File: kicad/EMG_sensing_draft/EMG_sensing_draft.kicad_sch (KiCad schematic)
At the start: 68 parts, among them J1 EMG_SIGNAL, J2 USB_A_0480370001, J3 DEBUG, U1 W25Q128JV, U2 RN4871-I/RM140, U3 RP2040, U4 MCP1702T-3302E_CB, U5 NCS4325DR2G, U6 MCP6021, U7 MCP6N11-002E/SN, Y1 12MHz

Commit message: restructured repo
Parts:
- removed C12: 0.1uF, symbol Device:C
- removed C13: 10uF, symbol Device:C
- removed C15: .33uF, symbol Device:C
- removed R21: 453, symbol Device:R
- removed R22: 200, symbol Device:R
- removed R23: 10k, symbol Device:R
- removed U5: NCS4325DR2G, SOIC14_4X8P75_ONS, symbol NCS4325DR2G:NCS4325DR2G
- added C17: 0.1uF, symbol Device:C
- added C21, C23: .33uF, symbol Device:C
- added C22: .033uF, symbol Device:C
- added R19: 9.09k, symbol Device:R
- added R25: 453, symbol Device:R
- added R26: 200, symbol Device:R
- added U7: MCP6024-I/P, PDIP14_300MC_MCH, symbol MCP6024:MCP6024-I/P
- C16: value .033uF -> 1uF
- C18: value .33uF -> 1uF
- C19: value 1uF -> .1uF
- C20: value .1uF -> 10uF
- R14: value 453 -> 10k
- R15: value 909 -> 453
- R16: value 8.1K -> 10k
- R17: value 9.09k -> 909
- R18: value 200 -> 8.1K
- R20: value 909 -> 200
- R24: value 10k -> 909
- renumbered C21 to C12, C22 to C13, C17 to C15, J2 to J1, J1 to J2, R25 to R10, R26 to R11, R19 to R12, R10 to R21, R11 to R22, R12 to R23, U2 to U1, U1 to U2, U7 to U4, U4 to U5
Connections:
- net +1.65V: now also R14.2, R15.1, R16.2, U7.12 (VIND+), U7.3 (VINA+); no longer R14.1, R24.2
- net +3.3V: now also C16.2, C18.1, C17.2, U7.4 (VDD); no longer C20.1
- net GND: now also R16.1, C17.1, C22.1, C23.2, U7.11 (VSS); no longer C20.2, R20.1
- net V_SIGNAL: now also C22.2, R19.2; no longer C16.2, R17.2
- net at R20.2: now also R26.1, U7.13 (VIND-); no longer C18.1
- net at R18.1: now also C20.2, U7.2 (VINA-); no longer R16.2
- net at R18.2: now also R20.1, U7.1 (VOUTA)
- net at R13.2: now also C20.1
- net at D7.2 (K): now also R26.2, U7.10 (VINC+)
- net at D7.1 (A): now also U7.14 (VOUTD)
- net at R15.2, R17.1: now also C21.1, U7.6 (VINB-)
- net at U6.1, U6.4: now also R14.1
- new net: C21.2, R17.2, R19.1, U7.7 (VOUTB)
- new net: C23.1, R24.2, R25.1, U7.5 (VINB+)
- new net: R25.2, U7.8 (VOUTC), U7.9 (VINC-)
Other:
- note added: "BANDPASS FILTER, RECTIFICATION, AND LEVEL SHIFTING"
- note added: "REFERENCE VOLTAGE"
- note removed: "BANDPASS FILTER AND RECTIFICATION"
- moved on the sheet: C12, C13, C14, C15, D1, D6, J1, J2, J3, R10, R11, R12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

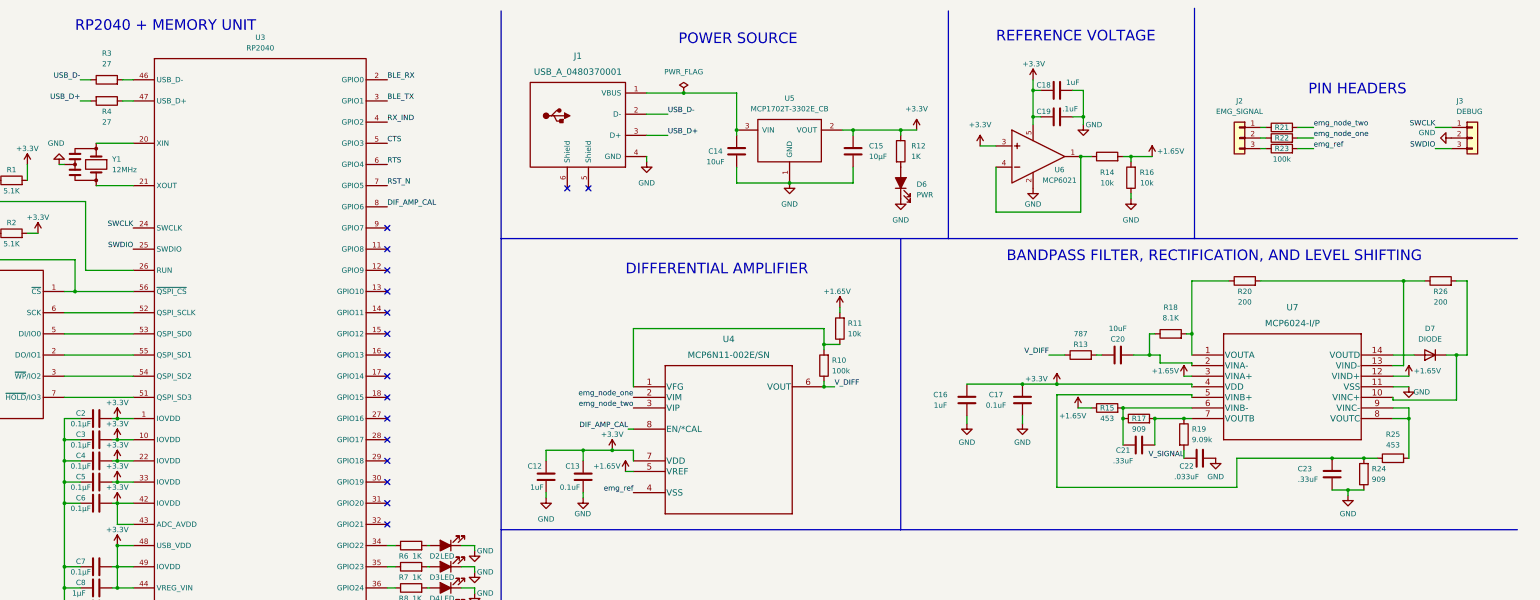
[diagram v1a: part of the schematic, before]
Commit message: fixed mcp6024 schematic symbol
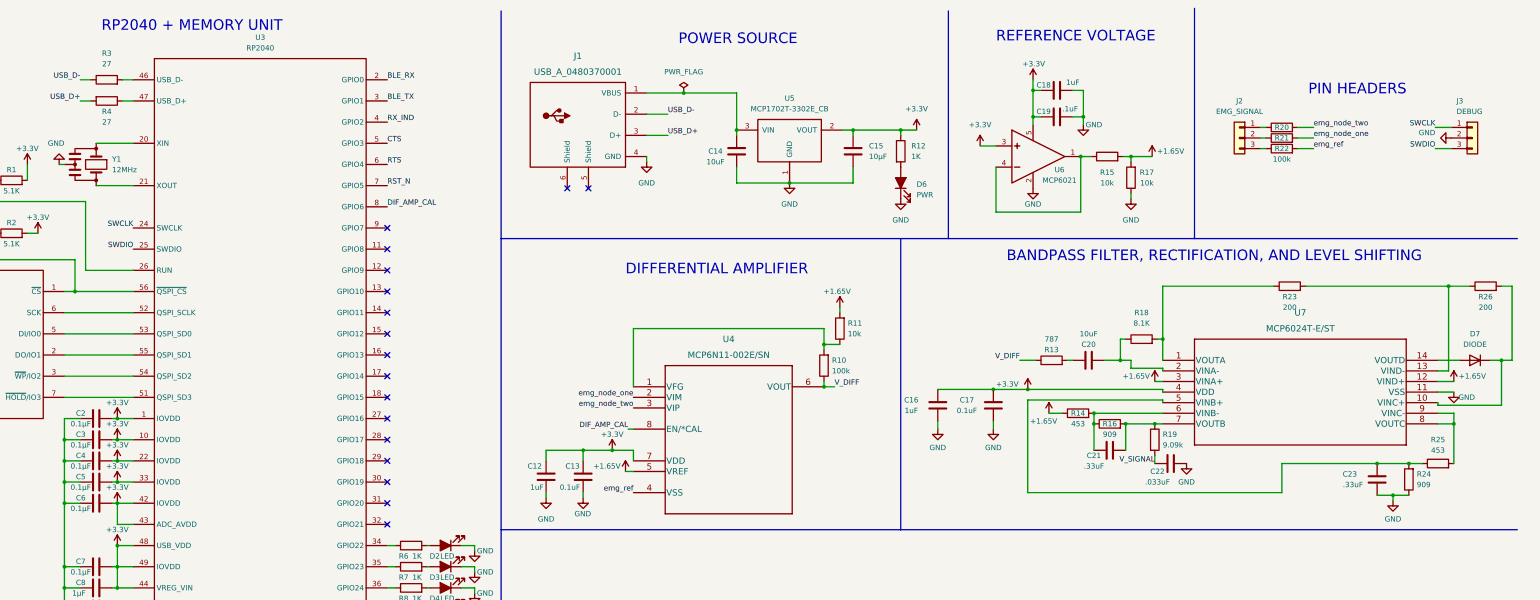
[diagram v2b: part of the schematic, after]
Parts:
- removed R15: 453, symbol Device:R
- removed R17: 909, symbol Device:R
- removed R20: 200, symbol Device:R
- removed U7: MCP6024-I/P, PDIP14_300MC_MCH, symbol MCP6024:MCP6024-I/P
- added R14: 453, symbol Device:R
- added R16: 909, symbol Device:R
- added R23: 200, symbol Device:R
- added U7: MCP6024T-E/ST, TSSOP14_MC_MCH, symbol MCP6024:MCP6024T-E/ST
- R20: renamed from R21; value R -> 100k
- R21: renamed from R22; value R -> 100k
- renumbered R14 to R15, R16 to R17, R23 to R22
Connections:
- net +1.65V: now also R14.1, U7.12 (VIND+), U7.3 (VINA+)
- net +3.3V: now also U7.4 (VDD)
- net GND: now also U7.11 (VSS)
- net at C20.2, R18.1: now also U7.2 (VINA-)
- net at R18.2: now also R23.1, U7.1 (VOUTA)
- net at C21.1: now also R14.2, R16.1, U7.6 (VINB-)
- net at C21.2, R19.1: now also R16.2, U7.7 (VOUTB)
- net at D7.2 (K), R26.2: now also U7.10 (VINC+)
- net at R26.1: now also R23.2, U7.13 (VIND-)
- net at D7.1 (A): now also U7.14 (VOUTD)
- net at C23.1, R24.2, R25.1: now also U7.5 (VINB+)
- net at R25.2: now also U7.8 (VOUTC), U7.9 (VINC-)

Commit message: added digital potentiometer
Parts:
- removed R11: 10k, symbol Device:R
- added U?: ISL90462WIH627Z-TKCT-ND, SOT23-6_INR, symbol ISL90462WIH627Z-TKCT-ND:ISL90462WIH627Z-TKCT-ND
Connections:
- net +1.65V: now also U?.6 (RH)
- net +3.3V: now also U?.1 (VDD)
- net GND: now also U?.2 (GND)
- net POT_CHANGE: now reaches U3.11 (GPIO8)
- net POT_CHANGE: now also U?.3 (U/*D)
- net POT_CS: now reaches U3.9 (GPIO7)
- net POT_CS: now also U?.4 (*CS)
- net at R10.2, U4.1 (VFG): now also U?.5 (RW)
- no-connect marks 25 -> 23
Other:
- moved on the sheet: C12, C13, D1, R10, R5, U1, U4

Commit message: linked schematic symbols to footprints
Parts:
- C1: renamed from C12; footprint (none) -> Capacitor_SMD:C_0603_1608Metric
- C10: renamed from C8; value 1µF -> 1uF; footprint Capacitor_SMD:C_0402_1005Metric -> Capacitor_SMD:C_0603_1608Metric
- C11: renamed from C9; value 1µF -> 1uF; footprint Capacitor_SMD:C_0402_1005Metric -> Capacitor_SMD:C_0603_1608Metric
- C12: renamed from C10; value 0.1µF -> 0.1uF; footprint Capacitor_SMD:C_0402_1005Metric -> Capacitor_SMD:C_0603_1608Metric
- C13: renamed from C11; value 0.1µF -> 0.1uF; footprint Capacitor_SMD:C_0402_1005Metric -> Capacitor_SMD:C_0603_1608Metric
- C14, C16, C17, C18, C19, C20, C21, C22, C23: footprint (none) -> Capacitor_SMD:C_0603_1608Metric
- C15: value 10µF -> 10uF
- C2: renamed from C1; value 0.1µF -> 0.1uF; footprint Resistor_SMD:R_0402_1005Metric -> Capacitor_SMD:C_0603_1608Metric
- C3: renamed from C13; footprint (none) -> Capacitor_SMD:C_0603_1608Metric
- C4: renamed from C2; value 0.1µF -> 0.1uF; footprint Capacitor_SMD:C_0402_1005Metric -> Capacitor_SMD:C_0603_1608Metric
- C5: renamed from C3; value 0.1µF -> 0.1uF; footprint Capacitor_SMD:C_0402_1005Metric -> Capacitor_SMD:C_0603_1608Metric
- C6: renamed from C4; value 0.1µF -> 0.1uF; footprint Capacitor_SMD:C_0402_1005Metric -> Capacitor_SMD:C_0603_1608Metric
- C7: renamed from C5; value 0.1µF -> 0.1uF; footprint Capacitor_SMD:C_0402_1005Metric -> Capacitor_SMD:C_0603_1608Metric
- C8: renamed from C6; value 0.1µF -> 0.1uF; footprint Capacitor_SMD:C_0402_1005Metric -> Capacitor_SMD:C_0603_1608Metric
- C9: renamed from C7; value 0.1µF -> 0.1uF; footprint Capacitor_SMD:C_0402_1005Metric -> Capacitor_SMD:C_0603_1608Metric
- D5: renamed from D1; footprint (none) -> LED_SMD:LED_0805_2012Metric
- J1: footprint (none) -> Eclectronics:USB_A_0480370001
- J2: footprint (none) -> Connector_PinHeader_2.54mm:PinHeader_1x03_P2.54mm_Vertical
- R1, R2: value 5.1K -> 5.1k; footprint Resistor_SMD:R_0402_1005Metric -> Resistor_SMD:R_0603_1608Metric
- R10: renamed from R5; footprint (none) -> Resistor_SMD:R_0603_1608Metric
- R11: renamed from R12; value 1K -> 1k; footprint Resistor_SMD:R_0402_1005Metric -> Resistor_SMD:R_0603_1608Metric
- R12: renamed from R13; footprint (none) -> Resistor_SMD:R_0603_1608Metric
- R13: renamed from R14; footprint (none) -> Resistor_SMD:R_0603_1608Metric
- R14: renamed from R15; footprint (none) -> Resistor_SMD:R_0603_1608Metric
- R15: renamed from R16; footprint (none) -> Resistor_SMD:R_0603_1608Metric
- R16: renamed from R17; footprint (none) -> Resistor_SMD:R_0603_1608Metric
- R17: renamed from R18; value 8.1K -> 8.1k; footprint (none) -> Resistor_SMD:R_0603_1608Metric
- R18: renamed from R19; footprint (none) -> Resistor_SMD:R_0603_1608Metric
- R19: renamed from R20; footprint (none) -> Resistor_SMD:R_0603_1608Metric
- R20: renamed from R21; footprint (none) -> Resistor_SMD:R_0603_1608Metric
- R21: renamed from R22; footprint (none) -> Resistor_SMD:R_0603_1608Metric
- R22: renamed from R23; footprint (none) -> Resistor_SMD:R_0603_1608Metric
- R23: renamed from R24; footprint (none) -> Resistor_SMD:R_0603_1608Metric
- R24: renamed from R25; footprint (none) -> Resistor_SMD:R_0603_1608Metric
- R25: renamed from R26; footprint (none) -> Resistor_SMD:R_0603_1608Metric
- R3, R4: footprint (none) -> Resistor_SMD:R_0603_1608Metric
- R5: renamed from R10; footprint (none) -> Resistor_SMD:R_0603_1608Metric
- R6, R7, R8, R9: value 1K -> 1k; footprint Resistor_SMD:R_0402_1005Metric -> Resistor_SMD:R_0603_1608Metric
- U1: renamed from U4; footprint SOIC8-N_MC_MCH -> MCP6N11:MCP6N11-002ESN
- U3: renamed from U?; footprint SOT23-6_INR -> ISL90462WIH627Z:ISL90462WIH627Z-TKCT-ND
- U4: renamed from U3; footprint (none) -> Eclectronics:RP2040
- U5: renamed from U1; footprint RN4871_MCH -> RN4871:RN4871
- U6: renamed from U5; footprint (none) -> Package_TO_SOT_SMD:SOT-23
- U7: renamed from U6; footprint (none) -> Package_TO_SOT_SMD:SOT-23-5
- U8: renamed from U7; footprint TSSOP14_MC_MCH -> MCP6024:MCP6024T
- renumbered D2 to D1, D3 to D2, D4 to D3, D5 to D4
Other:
- moved on the sheet: R22

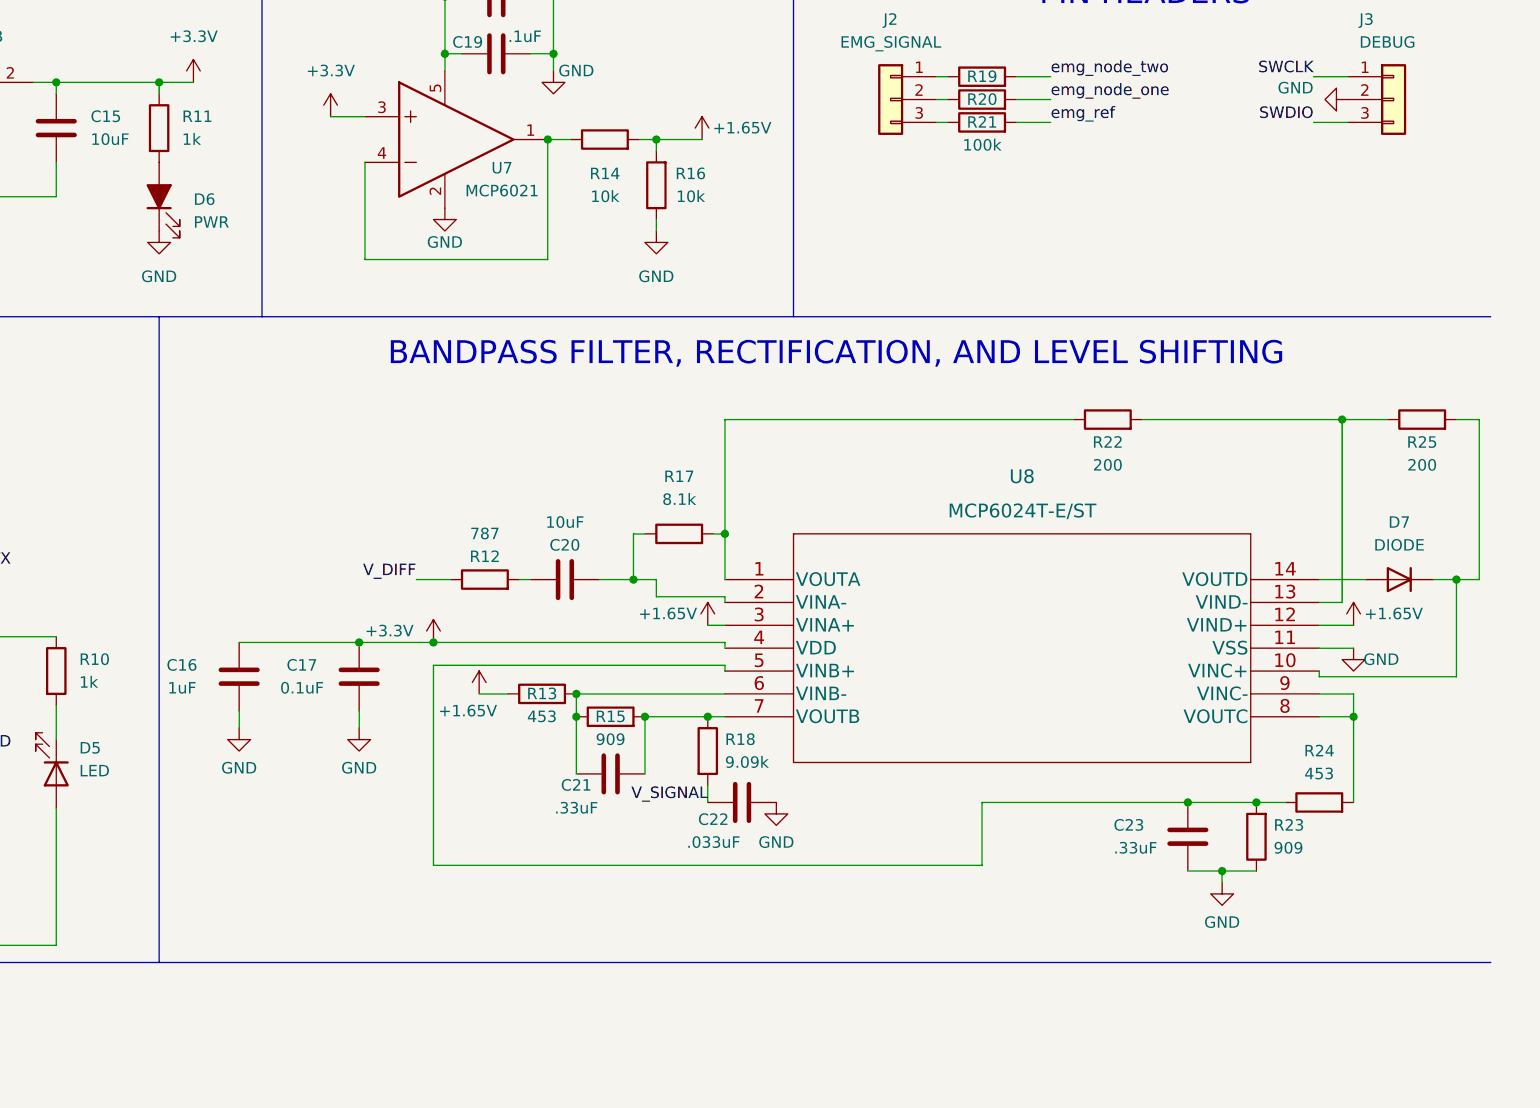
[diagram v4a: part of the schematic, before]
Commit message: fixed rectifier schematic
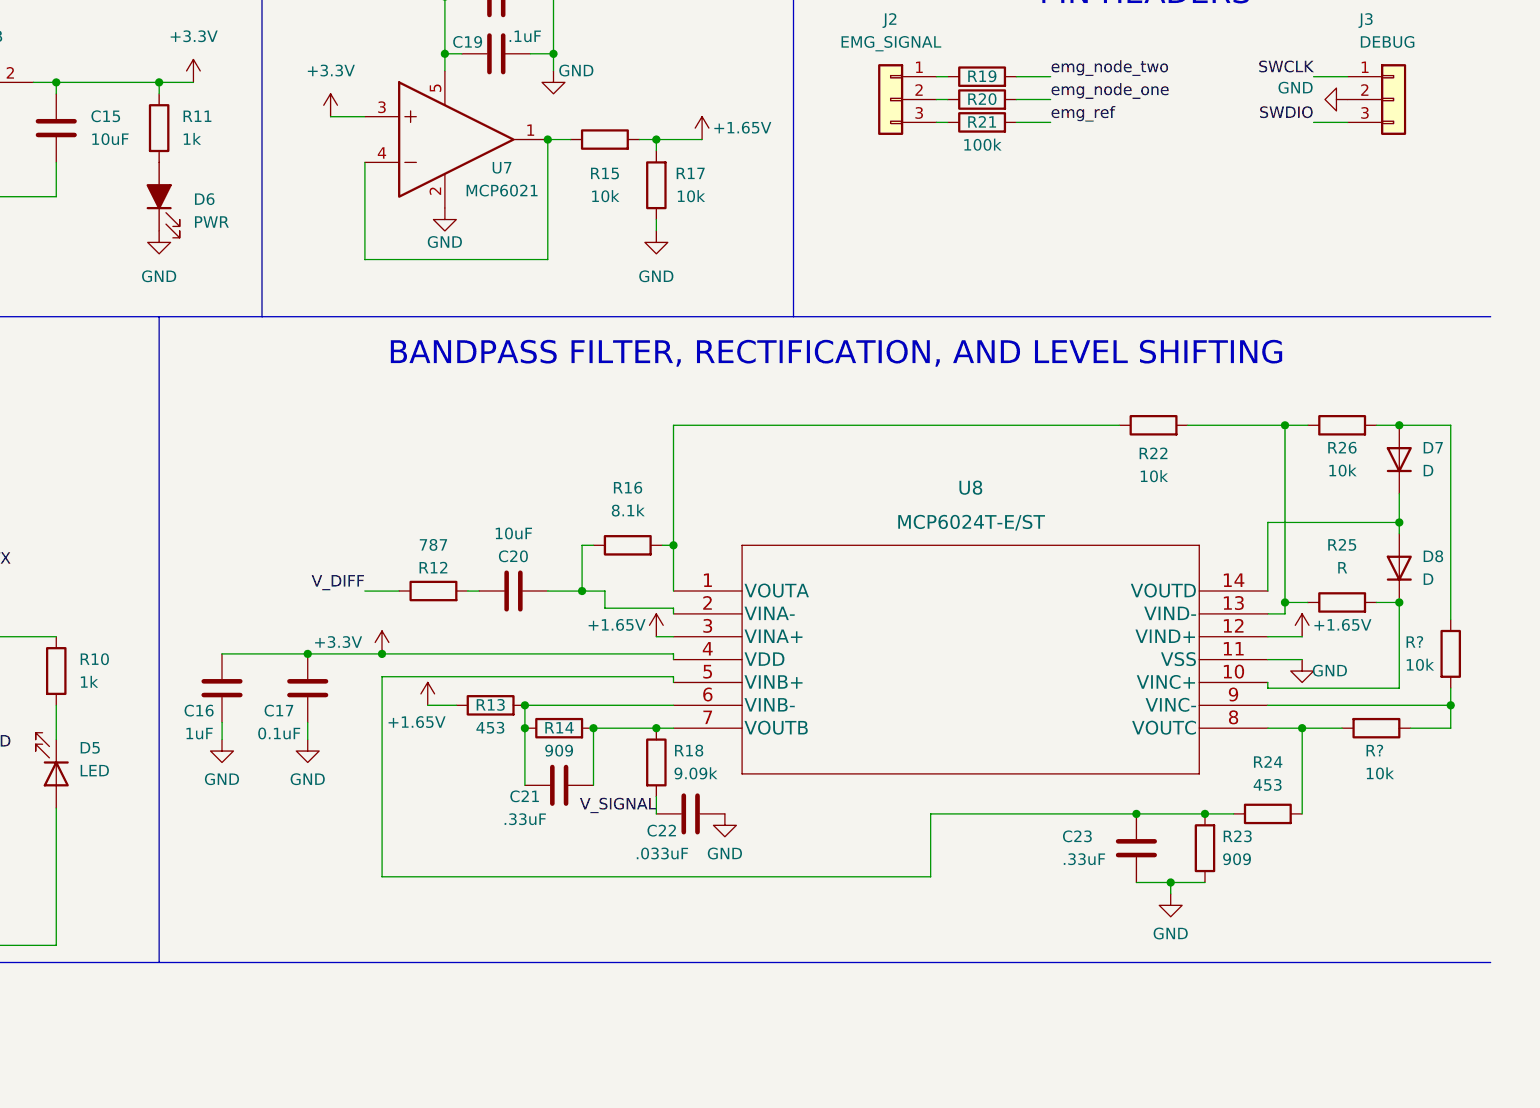
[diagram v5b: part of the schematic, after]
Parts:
- removed D7: DIODE, symbol Simulation_SPICE:DIODE
- added D7, D8: D, symbol Device:D
- added R26, R? (x2): 10k, symbol Device:R
- R22: value 200 -> 10k; footprint Resistor_SMD:R_0603_1608Metric -> (none)
- R25: value 200 -> R; footprint Resistor_SMD:R_0603_1608Metric -> (none)
- renumbered R15 to R14, R14 to R15, R17 to R16, R16 to R17
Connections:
- net at R24.2, U8.8 (VOUTC): now also R?.2; no longer U8.9 (VINC-)
- net at U8.14 (VOUTD): now also D7.1 (K), D8.2 (A)
- net at R25.2, U8.10 (VINC+): now also D8.1 (K)
- net at R22.2, R25.1, U8.13 (VIND-): now also R26.1
- new net: D7.2 (A), R26.2, R?.1
- new net: R?.1, R?.2, U8.9 (VINC-)
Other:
- moved on the sheet: C16, C17, C20, C21, C22, C23, R12, R13, R14, R16, R18, R23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

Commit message: Change schematics based on Brad's comments (incomplete)
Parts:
- removed U7: MCP6021, Package_TO_SOT_SMD:SOT-23-5, symbol Eclectronics:MCP6021
- added C? (x2): .33uF, Capacitor_SMD:C_0603_1608Metric, symbol Device:C
- added C?: 10uF, Capacitor_SMD:C_0603_1608Metric, symbol Device:C
- added C?: 1uF, Capacitor_SMD:C_0603_1608Metric, symbol Device:C
- added C? (x2): 0.1uF, Capacitor_SMD:C_0603_1608Metric, symbol Device:C
- added C?: .033uF, Capacitor_SMD:C_0603_1608Metric, symbol Device:C
- added D? (x2): D, symbol Device:D
- added R?: 8.1k, Resistor_SMD:R_0603_1608Metric, symbol Device:R
- added R? (x5): 10k, symbol Device:R
- added R? (x2): 453, Resistor_SMD:R_0603_1608Metric, symbol Device:R
- added R?: 787, Resistor_SMD:R_0603_1608Metric, symbol Device:R
- added R? (x2): 909, Resistor_SMD:R_0603_1608Metric, symbol Device:R
- added R?: 9.09k, Resistor_SMD:R_0603_1608Metric, symbol Device:R
- added U? (x5): Opamp_MCP6024T-E/ST, symbol Device:Opamp_MCP6024T-E/ST
- added U?: MCP6021, Package_TO_SOT_SMD:SOT-23-5, symbol Eclectronics:MCP6021
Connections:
- net +1.65V: now also R?.1, U?.1, U?.1 (VINA+), U?.1 (VINB+), U?.4; no longer R15.2, R17.2
- net +3.3V: now also R15.1, C?.1, C?.2, C?.2, U?. (VSS), U?.5
- net CTS: now also U4.4 (GPIO2); no longer U4.5 (GPIO3)
- net GND: now also U1.4 (VSS), C?.1, C?.1, C?.2, C?.2, U?. (VSS), U?.2
- net RX_IND: now also U4.5 (GPIO3); no longer U4.4 (GPIO2)
- net V_DIFF: now also R?.1
- net V_SIGNAL: now also C?.1, R?.2
- net emg_ref: no longer U1.4 (VSS)
- new net: C?.2, R?.1, U?.2 (VINA-)
- new net: R?.1, R?.2, U?.3 (VOUTA)
- new net: R15.2, R17.2, U?.3
- new net: R?.2, U?.2 (VINB-)
- new net: D?.1 (K), D?.2 (A), U?.3 (VOUTB)
- new net: C?.1, C?.2, R?.1, R?.1, R?.2, U?.3 (VOUTD)
- new net: C?.2, R?.2, R?.2, U?.1 (VIND+)
- new net: C?.1, R?.2
- new net: C?.1, R?.1, R?.2, U?.2 (VIND-)
- new net Vout_1: D?.2 (A), R?.1, R?.1, R?.1, R?.2
- new net Vout_2_neg: R?.1, R?.2, U?.2 (VINC-)
- new net Vout_2_pos: D?.1 (K), R?.2, U?.1 (VINC+)
- new net Vout_3: R?.1, R?.2, U?.3 (VOUTC)
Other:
- note added: "BANDPASS FILTER, RECTIFICATION, AND LEVEL SHIFTING 2"
- moved on the sheet: C18, C19, R15, R17
